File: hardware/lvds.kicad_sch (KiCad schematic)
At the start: 52 parts, among them U4 GateMate-CCGM1A1, Y1 ASE2-25.000MHZ-L-C-T

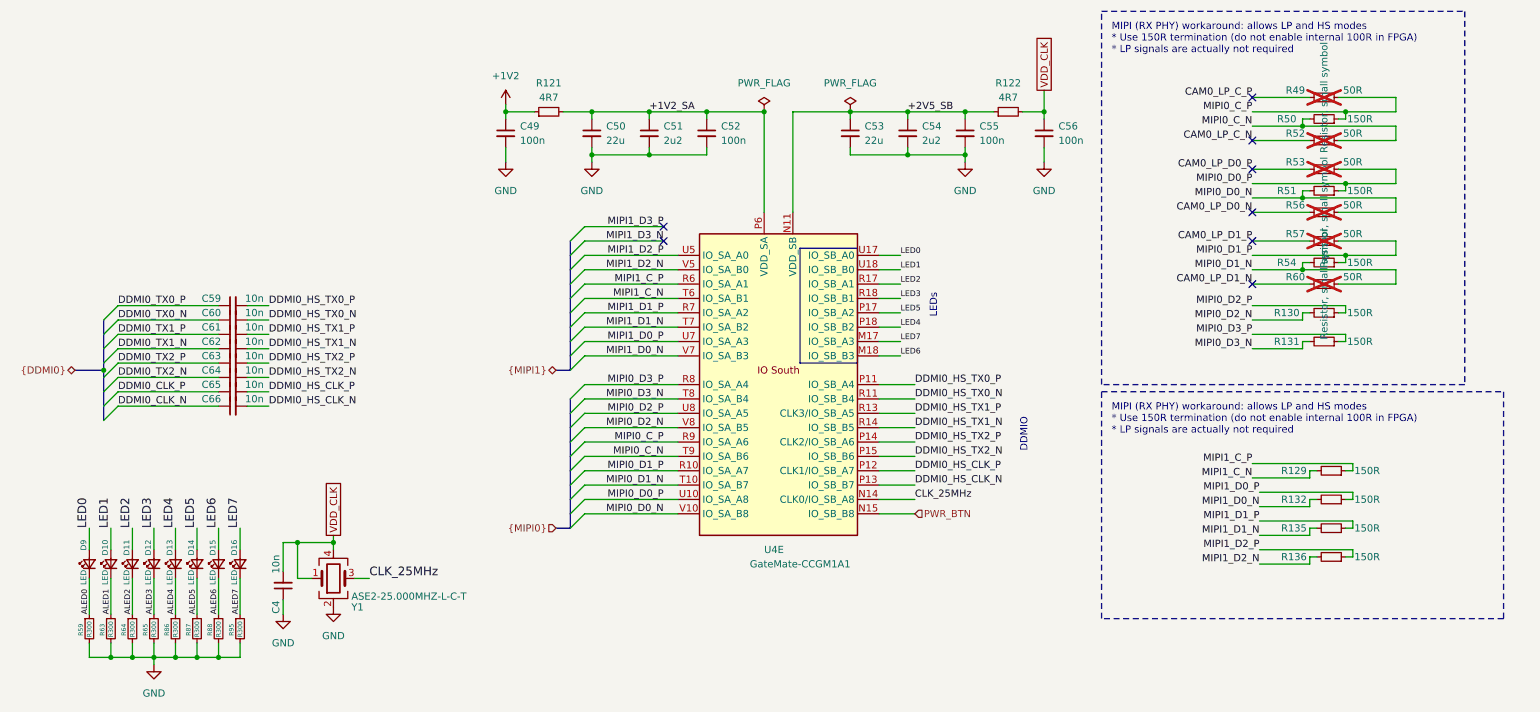
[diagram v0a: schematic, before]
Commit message: Updating sch - moving power select resistors to bottom
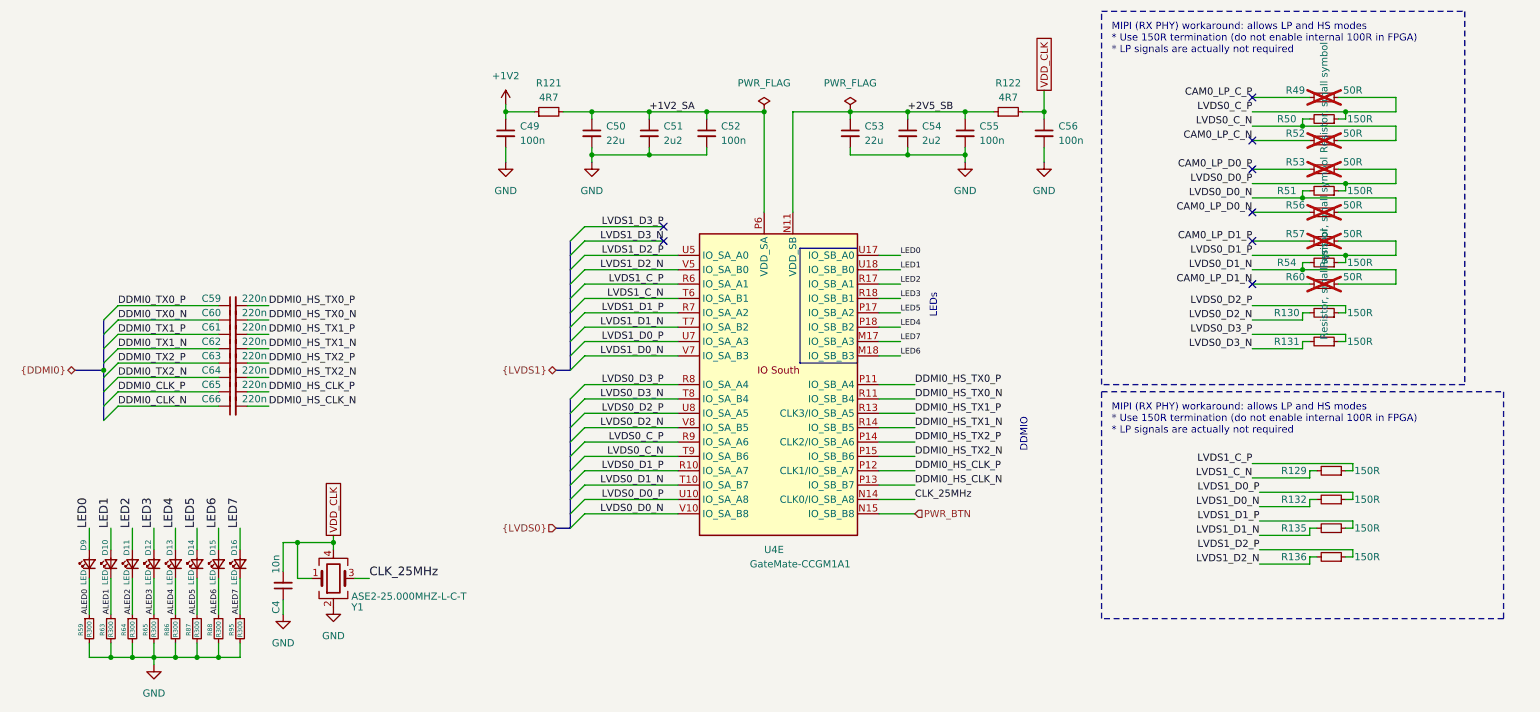
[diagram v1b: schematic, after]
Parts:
- C59, C60, C61, C62, C63, C64, C65, C66: value 10n -> 220n
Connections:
- net MIPI0_C_N renamed LVDS0_C_N
- net MIPI0_C_P renamed LVDS0_C_P
- net MIPI0_D0_N renamed LVDS0_D0_N
- net MIPI0_D0_P renamed LVDS0_D0_P
- net MIPI0_D1_N renamed LVDS0_D1_N
- net MIPI0_D1_P renamed LVDS0_D1_P
- net MIPI0_D2_N renamed LVDS0_D2_N
- net MIPI0_D2_P renamed LVDS0_D2_P
- net MIPI0_D3_N renamed LVDS0_D3_N
- net MIPI0_D3_P renamed LVDS0_D3_P
- net MIPI1_C_N renamed LVDS1_C_N
- net MIPI1_C_P renamed LVDS1_C_P
- net MIPI1_D0_N renamed LVDS1_D0_N
- net MIPI1_D0_P renamed LVDS1_D0_P
- net MIPI1_D1_N renamed LVDS1_D1_N
- net MIPI1_D1_P renamed LVDS1_D1_P
- net MIPI1_D2_N renamed LVDS1_D2_N
- net MIPI1_D2_P renamed LVDS1_D2_P

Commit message: Adding some tekst
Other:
- note added: "PWR_BTN needs internal PULL-UP"
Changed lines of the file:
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@@
+		)
+	)
+	(text "PWR_BTN\nneeds internal PULL-UP"
+		(exclude_from_sim no)
+		(at 188.214 106.426 0)
+		(effects
+			(font
+				(size 1.27 1.27)
+			)
 		)
 	)

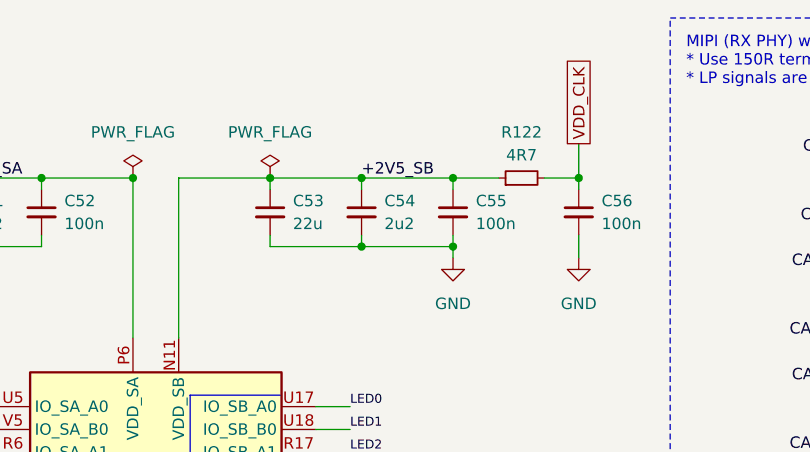
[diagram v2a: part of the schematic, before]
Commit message: Moving VDD_CLK to 1V8, removing 2V5
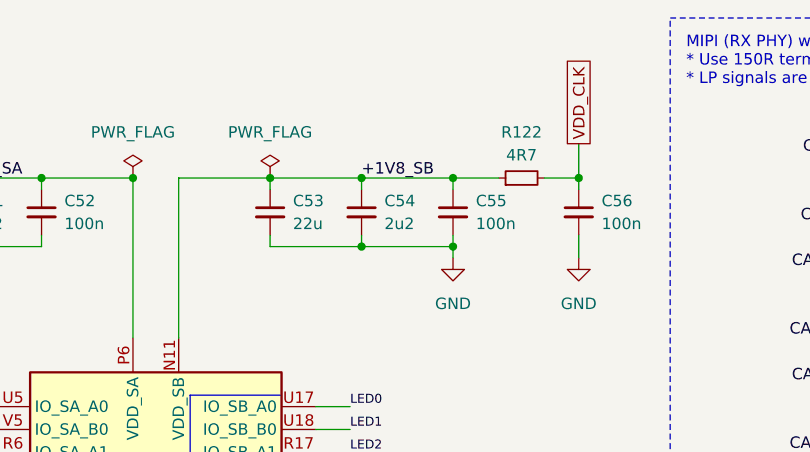
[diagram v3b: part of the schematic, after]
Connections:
- net +2V5_SB renamed +1V8_SB
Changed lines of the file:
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@@
 		)
 	)
-	(label "+2V5_SB"
+	(label "+1V8_SB"
 		(at 175.26 30.48 0)
 		(effects
@@
 			)
 		)
-		(property "Description" "Power symbol creates a global label with name \"+2V5\""
+		(property "Description" "Power symbol creates a global label with name \"+1V2\""
+			(at 104.14 29.21 0)
+			(effects
+				(font
+					(size 1.27 1.27)
+				)
+				(hide yes)
+			)
+		)
+		(property "LCSC" ""
 			(at 104.14 29.21 0)
 			(effects

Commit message: CleanUP
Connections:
- net PWR_BTN renamed RST_N
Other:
- note removed: "PWR_BTN needs internal PULL-UP"
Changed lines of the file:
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@@
 		)
 	)
-	(text "PWR_BTN\nneeds internal PULL-UP"
-		(exclude_from_sim no)
-		(at 188.214 106.426 0)
-		(effects
-			(font
-				(size 1.27 1.27)
-			)
-		)
-	)
 	(junction
 		(at 119.38 38.1)
@@
 		)
 	)
+	(global_label "RST_N"
+		(shape input)
+		(at 176.53 101.6 0)
+		(fields_autoplaced yes)
+		(effects
+			(font
+				(size 1.27 1.27)
+			)
+			(justify left)
+		)
+		(property "Intersheetrefs" "${INTERSHEET_REFS}"
+			(at 185.2604 101.6 0)
+			(effects
+				(font
+					(size 1.27 1.27)
+				)
+				(justify left)
+				(hide yes)
+			)
+		)
+	)
 	(hierarchical_label "{LVDS1}"
 		(shape bidirectional)
@@
 		)
 	)
-	(hierarchical_label "PWR_BTN"
-		(shape input)
-		(at 176.53 101.6 0)
-		(effects
-			(font
-				(size 1.254 1.254)
-			)
-			(justify left)
-		)
-	)
